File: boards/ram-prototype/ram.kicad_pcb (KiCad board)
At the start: 4 copper layers, 173 x 118 mm, 611 parts, among them J1 PinHeader_1x24_P2.54mm_Vertic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, J2 PinHeader_1x04_P2.54mm_Vertic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, J3 PinHeader_1x14_P2.54mm_Vertic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, J4 PinHeader_2x08_P2.54mm_Vertic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, U1 DSBGA\-5_NumericPads, U10 DSBGA\-5_NumericPads, U100 DSBGA\-5_NumericPads, U101 DSBGA\-5_NumericPads, U102 DSBGA\-5_NumericPads, U103 DSBGA\-5_NumericPads, U104 DSBGA\-5_NumericPads, U105 DSBGA\-5_NumericPads, U106 DSBGA\-5_NumericPads, U107 DSBGA\-5_NumericPads, U108 DSBGA\-5_NumericPads, U109 DSBGA\-5_NumericPads, U11 DSBGA\-5_NumericPads, U110 DSBGA\-5_NumericPads, U111 DSBGA\-5_NumericPads, U112 DSBGA\-5_NumericPads, U113 DSBGA\-5_NumericPads, U114 DSBGA\-5_NumericPads, U115 DSBGA\-5_NumericPads, U116 DSBGA\-5_NumericPads, U117 DSBGA\-5_NumericPads, U118 DSBGA\-5_NumericPads, U119 DSBGA\-5_NumericPads, U12 DSBGA\-5_NumericPads, U120 DSBGA\-5_NumericPads, U121 DSBGA\-5_NumericPads, U122 DSBGA\-5_NumericPads, U123 DSBGA\-5_NumericPads, U124 DSBGA\-5_NumericPads, U125 DSBGA\-5_NumericPads, U126 DSBGA\-5_NumericPads, U127 DSBGA\-5_NumericPads, U128 DSBGA\-5_NumericPads, U129 DSBGA\-5_NumericPads, U13 DSBGA\-5_NumericPads, U130 DSBGA\-5_NumericPads, U131 DSBGA\-5_NumericPads, U132 DSBGA\-5_NumericPads, U133 DSBGA\-5_NumericPads, U134 DSBGA\-5_NumericPads, U135 DSBGA\-5_NumericPads, U136 DSBGA\-5_NumericPads, U137 DSBGA\-5_NumericPads, U138 DSBGA\-5_NumericPads, U139 DSBGA\-5_NumericPads, U14 DSBGA\-5_NumericPads, U140 DSBGA\-5_NumericPads, U141 DSBGA\-5_NumericPads, U142 DSBGA\-5_NumericPads, U143 DSBGA\-5_NumericPads, U144 DSBGA\-5_NumericPads, U145 DSBGA\-5_NumericPads, U146 DSBGA\-5_NumericPads, U147 DSBGA\-5_NumericPads, U148 DSBGA\-5_NumericPads, U149 DSBGA\-5_NumericPads, U15 DSBGA\-5_NumericPads, U150 DSBGA\-5_NumericPads, U151 DSBGA\-5_NumericPads, U152 DSBGA\-5_NumericPads, U153 DSBGA\-5_NumericPads, U154 DSBGA\-5_NumericPads, U155 DSBGA\-5_NumericPads, U156 DSBGA\-5_NumericPads, U157 DSBGA\-5_NumericPads, U158 DSBGA\-5_NumericPads, U159 DSBGA\-5_NumericPads, U16 DSBGA\-5_NumericPads, U160 DSBGA\-5_NumericPads, U161 DSBGA\-5_NumericPads, U162 DSBGA\-5_NumericPads, U163 DSBGA\-5_NumericPads, U164 DSBGA\-5_NumericPads, U165 DSBGA\-5_NumericPads, U166 DSBGA\-5_NumericPads, U167 DSBGA\-5_NumericPads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

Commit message: route D* bus above control logic, restore A7-A10 prerouting
- Move ctrl_logic down 7mm below decoder (CTRL_DBUS_GAP=7.0) to create
  a corridor for the D* bus between decoder bottom and ctrl_logic top
- D* bus corridor at y≈102-106, ctrl_logic at y≈110, A7-A10 below both
- Add obs_y_max filter to preroute_dbus_to_connector so it ignores
  ctrl_logic footprints when computing bus corridor Y
- Restrict obstacle scan to decoder area (x>35) to avoid connector LEDs
- Re-enable A7-A10 prerouting (now clears ctrl_logic)
- Update connector silkscreen labels for swapped pin assignment

Co-Authored-By: Claude Opus 4.6 (1M context) <noreply@anthropic.com>
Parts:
- moved D187 6.90 mm to (47.4, 110.2)
- moved D188 6.90 mm to (52.9, 110.2)
- moved D189 6.90 mm to (58.4, 110.2)
- moved D190 6.90 mm to (52.9, 114.2)
- moved D191 6.90 mm to (47.4, 114.2)
- moved D192 6.90 mm to (58.4, 114.2)
- moved R190 6.90 mm to (48.7, 110.2)
- moved R191 6.90 mm to (54.2, 110.2)
- moved R192 6.90 mm to (59.7, 110.2)
- moved R193 6.90 mm to (54.2, 114.2)
- moved R194 6.90 mm to (48.7, 114.2)
- moved R195 6.90 mm to (59.7, 114.2)
- moved U221 6.90 mm to (45.9, 110.2)
- moved U222 6.90 mm to (51.4, 110.2)
- moved U223 6.90 mm to (56.9, 110.2)
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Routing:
- net /D7: track 100.0 -> 178.4 mm
- net /D6: track 104.5 -> 182.1 mm
- net /D5: track 108.9 -> 185.7 mm
- net /D4: track 113.4 -> 189.4 mm
- net /D3: track 117.9 -> 193.1 mm
- net /D0: track 131.3 -> 206.2 mm
- net /D2: track 122.4 -> 196.8 mm
- net /D1: track 126.8 -> 201.0 mm

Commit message: regenerate all schematics and PCB from scripts
Freshly generated to ensure consistency after rebase.
0 ERC errors/warnings, 0 DRC errors/warnings.

Co-Authored-By: Claude Opus 4.6 (1M context) <noreply@anthropic.com>
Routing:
- net /WRITE_ACTIVE: track 2.67 -> 23.1 mm, vias 0 -> 4
- net /Address Decoder/A0: track 11.6 -> 14.1 mm
- net /Column Select/GA3: track 2.67 -> 4.67 mm
- net /Column Select/GA2: track 2.67 -> 4.67 mm
- net /Column Select/GA1: track 2.67 -> 4.67 mm
- net /Column Select/GA0: track 2.67 -> 4.67 mm
- net /Address Decoder/nA0: track 2.67 -> 4.67 mm
- net /Address Decoder/HA3: track 2.67 -> 4.67 mm
- net /Address Decoder/HA2: track 2.67 -> 4.67 mm
- net /Address Decoder/HA1: track 2.67 -> 4.67 mm
- net /Address Decoder/HA0: track 2.66 -> 4.66 mm
- net /Address Decoder/DEC4_0: track 2.66 -> 4.66 mm
- net /Column Select/A9: track 96.5 -> 98.0 mm
- net /Column Select/A7: track 96.5 -> 98.0 mm
- net /Address Decoder/A5: track 11.6 -> 13.1 mm
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
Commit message: route WRITE_ACTIVE and READ_EN vertical trunks on In1.Cu
Add preroute_ctrl_enable_trunks: routes both control enable signals
from row_ctrl AND gates on In1.Cu vertical trunks.

WRITE_ACTIVE trunk at ic_center_x with gaps where READ_EN horizontal
jogs cross. READ_EN trunk at ic_x+1.24 under the LED+R area. Both
use 0.34mm F.Cu escape stubs from pin 1 to vias with
remove_unused_layers. 8 vias + 25 traces total.

Also adds center escape for DSBGA-5 pin 2 (B1->B2 gap) on AND/INV
ICs (skipping control_logic and row_ctrl groups), and
remove_unused_layers parameter to PCBBuilder.pin_to_via().

0 errors, 0 warnings across Default/PCBWay/Elecrow rulesets.

Co-Authored-By: Claude Opus 4.6 (1M context) <noreply@anthropic.com>
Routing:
- net /READ_EN: track 2.67 -> 24.6 mm, vias 0 -> 4
- net /WRITE_ACTIVE: track 23.1 -> 18.7 mm
- net /nWE: track 12.6 -> 11.6 mm
- net /Address Decoder/ROW_SEL_3: track 3.67 -> 2.67 mm
- net /Address Decoder/ROW_SEL_2: track 3.67 -> 2.67 mm
- net /Address Decoder/ROW_SEL_1: track 3.66 -> 2.66 mm
- net /Address Decoder/ROW_SEL_0: track 3.66 -> 2.66 mm
- net Net-(D189-A): track 3.17 -> 2.67 mm
- net Net-(D188-A): track 3.17 -> 2.67 mm
- net /nOE: track 12.1 -> 11.6 mm
- net /nCE: track 12.1 -> 11.6 mm

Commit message: add pin 2 escape stubs for row_ctrl/control_logic, fix WRITE_ACTIVE trunk, improve FreeRouting clearances
- Remove skip of control_logic and row_ctrl ICs from preroute_center_escape
  so pin 2 (middle ball) gets escape stubs — reduces unconnected items from
  176 to 15
- Move READ_EN vias right of WRITE_ACTIVE trunk so horizontal jogs don't
  cross it, making WRITE_ACTIVE one uninterrupted vertical line
- Add Connectors net class for J2/J3/J4 secondary headers in .kicad_pro
- Fix DSN clearances: smd_smd 37.5µm→150µm, add via_via/via_smd/via_pin
  250µm to match KiCad DRC settings
- Increase verify timeout from 120s to 600s

Co-Authored-By: Claude Opus 4.6 (1M context) <noreply@anthropic.com>
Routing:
- net /WRITE_ACTIVE: track 18.7 -> 21.7 mm
- net /nWE: track 11.6 -> 12.6 mm
- net /Address Decoder/ROW_SEL_3: track 2.67 -> 3.67 mm
- net /Address Decoder/ROW_SEL_2: track 2.67 -> 3.67 mm
- net /Address Decoder/ROW_SEL_1: track 2.66 -> 3.66 mm
- net /Address Decoder/ROW_SEL_0: track 2.66 -> 3.66 mm
- net /READ_EN: track 24.6 -> 24.0 mm
- net Net-(D189-A): track 2.67 -> 3.17 mm
- net Net-(D188-A): track 2.67 -> 3.17 mm
- net /nOE: track 11.6 -> 12.1 mm
- net /nCE: track 11.6 -> 12.1 mm
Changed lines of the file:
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@@
   (segment (start 73.11 72.01) (end 72.61 72.01) (width 0.2) (layer "F.Cu") (net 12))
   (segment (start 73.11 77.56) (end 72.61 77.56) (width 0.2) (layer "F.Cu") (net 12))
+  (segment (start 86.41 60.91) (end 85.91 60.91) (width 0.2) (layer "F.Cu") (net 25))
+  (segment (start 86.41 63.21) (end 85.91 63.21) (width 0.2) (layer "F.Cu") (net 25))
+  (segment (start 86.41 66.46) (end 85.91 66.46) (width 0.2) (layer "F.Cu") (net 26))
+  (segment (start 86.41 68.76) (end 85.91 68.76) (width 0.2) (layer "F.Cu") (net 26))
+  (segment (start 86.41 72.01) (end 85.91 72.01) (width 0.2) (layer "F.Cu") (net 27))
+  (segment (start 86.41 74.31) (end 85.91 74.31) (width 0.2) (layer "F.Cu") (net 27))
+  (segment (start 86.41 77.56) (end 85.91 77.56) (width 0.2) (layer "F.Cu") (net 28))
+  (segment (start 86.41 79.86) (end 85.91 79.86) (width 0.2) (layer "F.Cu") (net 28))
+  (segment (start 46.11 110.23) (end 45.61 110.23) (width 0.2) (layer "F.Cu") (net 102))
+  (segment (start 51.61 110.23) (end 51.11 110.23) (width 0.2) (layer "F.Cu") (net 103))
+  (segment (start 57.11 110.23) (end 56.61 110.23) (width 0.2) (layer "F.Cu") (net 104))
+  (segment (start 46.11 114.23) (end 45.61 114.23) (width 0.2) (layer "F.Cu") (net 382))
+  (segment (start 51.61 114.23) (end 51.11 114.23) (width 0.2) (layer "F.Cu") (net 380))
+  (segment (start 57.11 114.23) (end 56.61 114.23) (width 0.2) (layer "F.Cu") (net 104))
   (segment (start 127.86 113.75) (end 127.86 114.25) (width 0.2) (layer "F.Cu") (net 52))
   (segment (start 131.86 113.75) (end 131.86 114.25) (width 0.2) (layer "F.Cu") (net 53))
@@
   (via (at 86.41 80.7) (size 0.5) (drill 0.3) (layers "F.Cu" "In1.Cu") (remove_unused_layers yes) (net 97))
   (segment (start 86.41 80.7) (end 86.16 80.7) (width 0.16) (layer "In1.Cu") (net 97))
-  (segment (start 86.41 61.41) (end 86.41 61.75) (width 0.2) (layer "F.Cu") (net 92))
-  (via (at 86.41 61.75) (size 0.5) (drill 0.3) (layers "F.Cu" "In1.Cu") (remove_unused_layers yes) (net 92))
-  (segment (start 86.41 61.75) (end 87.4 61.75) (width 0.16) (layer "In1.Cu") (net 92))
-  (segment (start 86.41 66.96) (end 86.41 67.3) (width 0.2) (layer "F.Cu") (net 92))
-  (via (at 86.41 67.3) (size 0.5) (drill 0.3) (layers "F.Cu" "In1.Cu") (remove_unused_layers yes) (net 92))
-  (segment (start 86.41 67.3) (end 87.4 67.3) (width 0.16) (layer "In1.Cu") (net 92))
-  (segment (start 86.41 72.51) (end 86.41 72.85) (width 0.2) (layer "F.Cu") (net 92))
-  (via (at 86.41 72.85) (size 0.5) (drill 0.3) (layers "F.Cu" "In1.Cu") (remove_unused_layers yes) (net 92))
-  (segment (start 86.41 72.85) (end 87.4 72.85) (width 0.16) (layer "In1.Cu") (net 92))
-  (segment (start 86.41 78.06) (end 86.41 78.4) (width 0.2) (layer "F.Cu") (net 92))
-  (via (at 86.41 78.4) (size 0.5) (drill 0.3) (layers "F.Cu" "In1.Cu") (remove_unused_layers yes) (net 92))
-  (segment (start 86.41 78.4) (end 87.4 78.4) (width 0.16) (layer "In1.Cu") (net 92))
-  (segment (start 86.16 64.05) (end 86.16 66.81) (width 0.16) (layer "In1.Cu") (net 97))
-  (segment (start 86.16 67.79) (end 86.16 69.6) (width 0.16) (layer "In1.Cu") (net 97))
-  (segment (start 86.16 69.6) (end 86.16 72.36) (width 0.16) (layer "In1.Cu") (net 97))
-  (segment (start 86.16 73.34) (end 86.16 75.15) (width 0.16) (layer "In1.Cu") (net 97))
-  (segment (start 86.16 75.15) (end 86.16 77.91) (width 0.16) (layer "In1.Cu") (net 97))
-  (segment (start 86.16 78.89) (end 86.16 80.7) (width 0.16) (layer "In1.Cu") (net 97))
+  (segment (start 86.41 61.41) (end 86.66 61.75) (width 0.2) (layer "F.Cu") (net 92))
+  (via (at 86.66 61.75) (size 0.5) (drill 0.3) (layers "F.Cu" "In1.Cu") (remove_unused_layers yes) (net 92))
+  (segment (start 86.66 61.75) (end 87.4 61.75) (width 0.16) (layer "In1.Cu") (net 92))
+  (segment (start 86.41 66.96) (end 86.66 67.3) (width 0.2) (layer "F.Cu") (net 92))
+  (via (at 86.66 67.3) (size 0.5) (drill 0.3) (layers "F.Cu" "In1.Cu") (remove_unused_layers yes) (net 92))
+  (segment (start 86.66 67.3) (end 87.4 67.3) (width 0.16) (layer "In1.Cu") (net 92))
+  (segment (start 86.41 72.51) (end 86.66 72.85) (width 0.2) (layer "F.Cu") (net 92))
+  (via (at 86.66 72.85) (size 0.5) (drill 0.3) (layers "F.Cu" "In1.Cu") (remove_unused_layers yes) (net 92))
+  (segment (start 86.66 72.85) (end 87.4 72.85) (width 0.16) (layer "In1.Cu") (net 92))
+  (segment (start 86.41 78.06) (end 86.66 78.4) (width 0.2) (layer "F.Cu") (net 92))
+  (via (at 86.66 78.4) (size 0.5) (drill 0.3) (layers "F.Cu" "In1.Cu") (remove_unused_layers yes) (net 92))
+  (segment (start 86.66 78.4) (end 87.4 78.4) (width 0.16) (layer "In1.Cu") (net 92))
+  (segment (start 86.16 64.05) (end 86.16 69.6) (width 0.16) (layer "In1.Cu") (net 97))
+  (segment (start 86.16 69.6) (end 86.16 75.15) (width 0.16) (layer "In1.Cu") (net 97))
+  (segment (start 86.16 75.15) (end 86.16 80.7) (width 0.16) (layer "In1.Cu") (net 97))
   (segment (start 87.4 61.75) (end 87.4 67.3) (width 0.16) (layer "In1.Cu") (net 92))
   (segment (start 87.4 67.3) (end 87.4 72.85) (width 0.16) (layer "In1.Cu") (net 92))

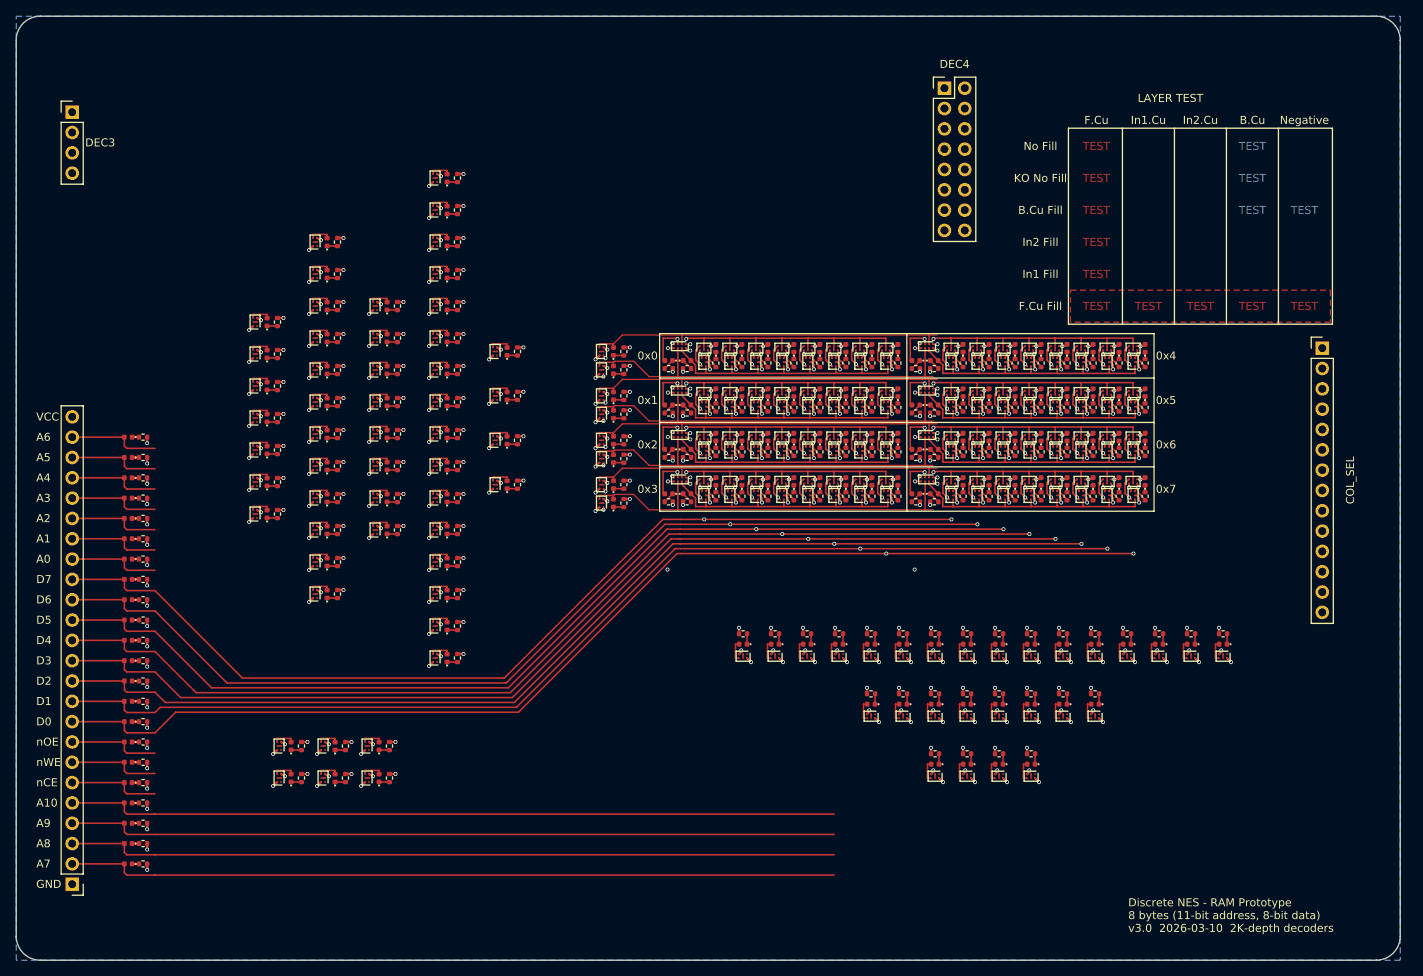
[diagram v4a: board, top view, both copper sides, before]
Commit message: fix pad coordinate precision, extend ram keepout, match fab clearance rules
- Increase get_pad_position() and add_trace() precision from 2 to 3 decimals
  (0.01mm -> 0.001mm). Fixes 5µm mismatch between trace endpoints and DSBGA
  pad positions that caused dangling track cleanup to delete NAND LED traces
- Extend ram_grid routing keepout to cover D* bus horizontal traces below
  byte grid (y2: 81.38 -> 86.67), stops before COL_SEL vias
- Match DSN clearances to actual PCBWay/Elecrow fab rules: via-to-track and
  via-to-via use 10mil (0.254mm) not 0.25mm. Eliminates all hole_clearance
  DRC violations. Post-routing errors: 271 -> 36

Co-Authored-By: Claude Opus 4.6 (1M context) <noreply@anthropic.com>
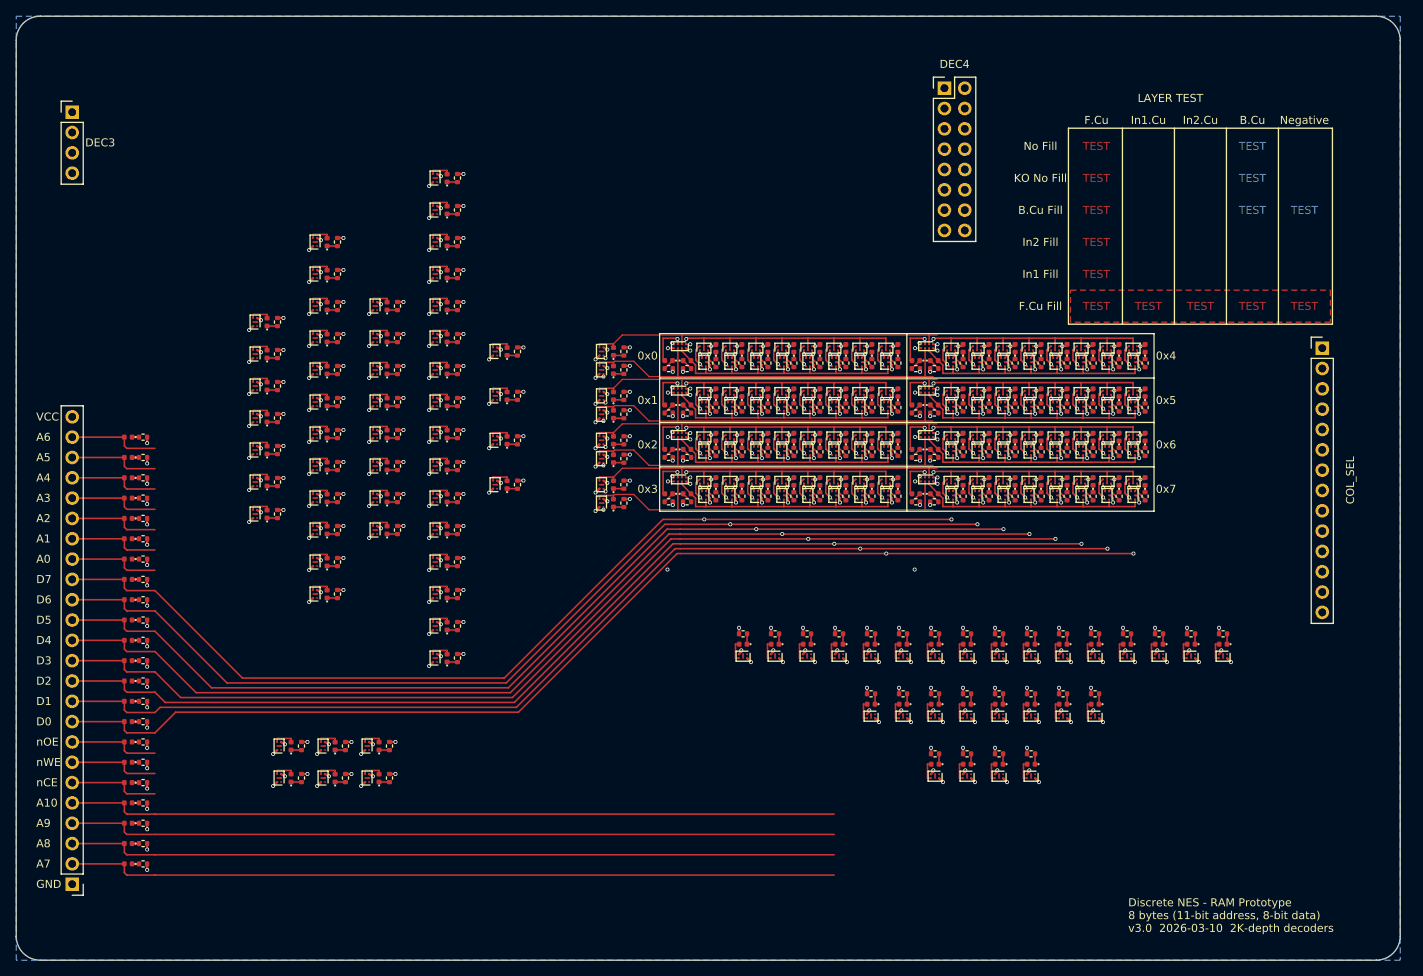
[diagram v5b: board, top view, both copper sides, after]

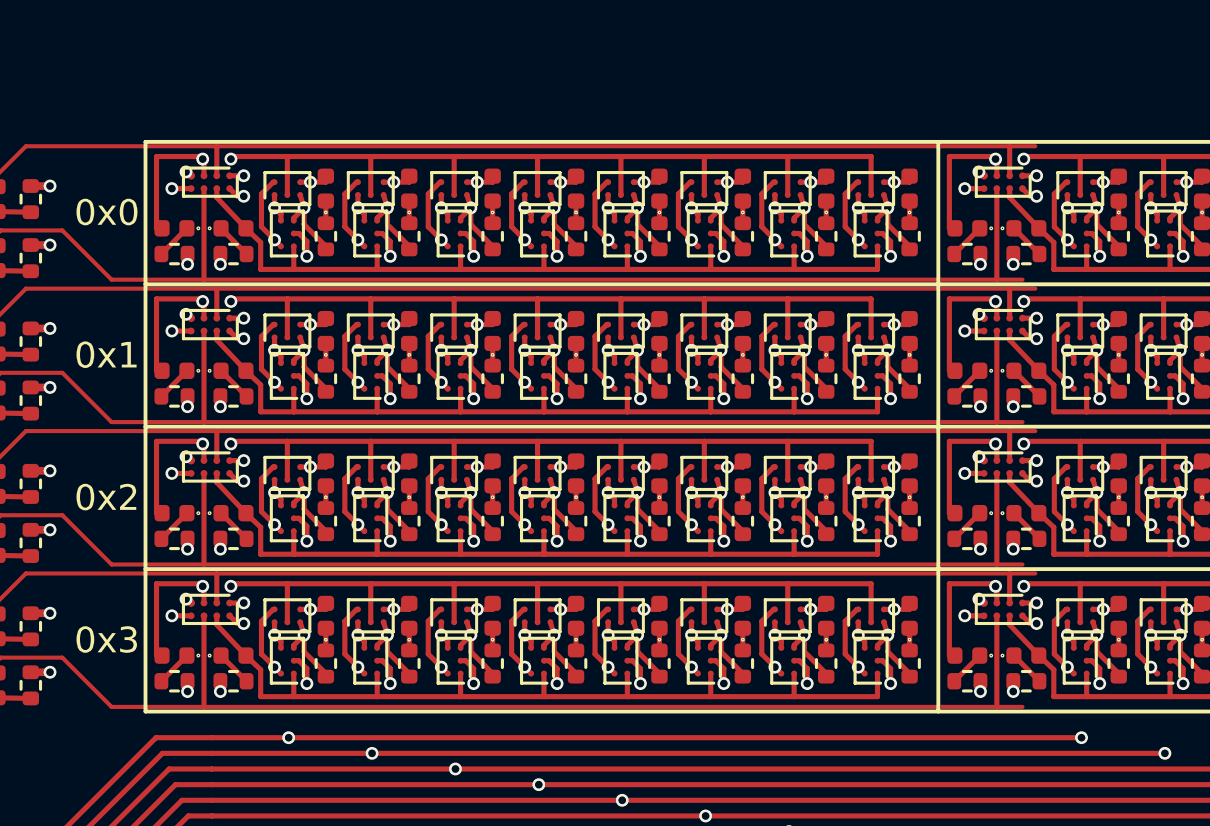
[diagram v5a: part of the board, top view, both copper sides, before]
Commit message: fix NAND LED anode route, COL_SEL trunk gap, and pad index precision
- Fix CLK LED approach route: T-branch from clk_pos[0] instead of
  clk_via_x (0.05mm gap caused dangling cleanup to delete LED route)
- Fix COL_SEL trunk extension: use actual bottom pin Y from
  get_pad_position() instead of hardcoded crtyd_bot_y (0.55mm gap)
- Increase _build_net_pad_index precision to 3 decimals to match
  get_pad_position/add_trace precision
- Save raw post-SES-import PCB to verify_output/ for inspection
- Post-routing: 36 errors -> 3 (1 nCE unconnected + 2 solder mask)

Co-Authored-By: Claude Opus 4.6 (1M context) <noreply@anthropic.com>
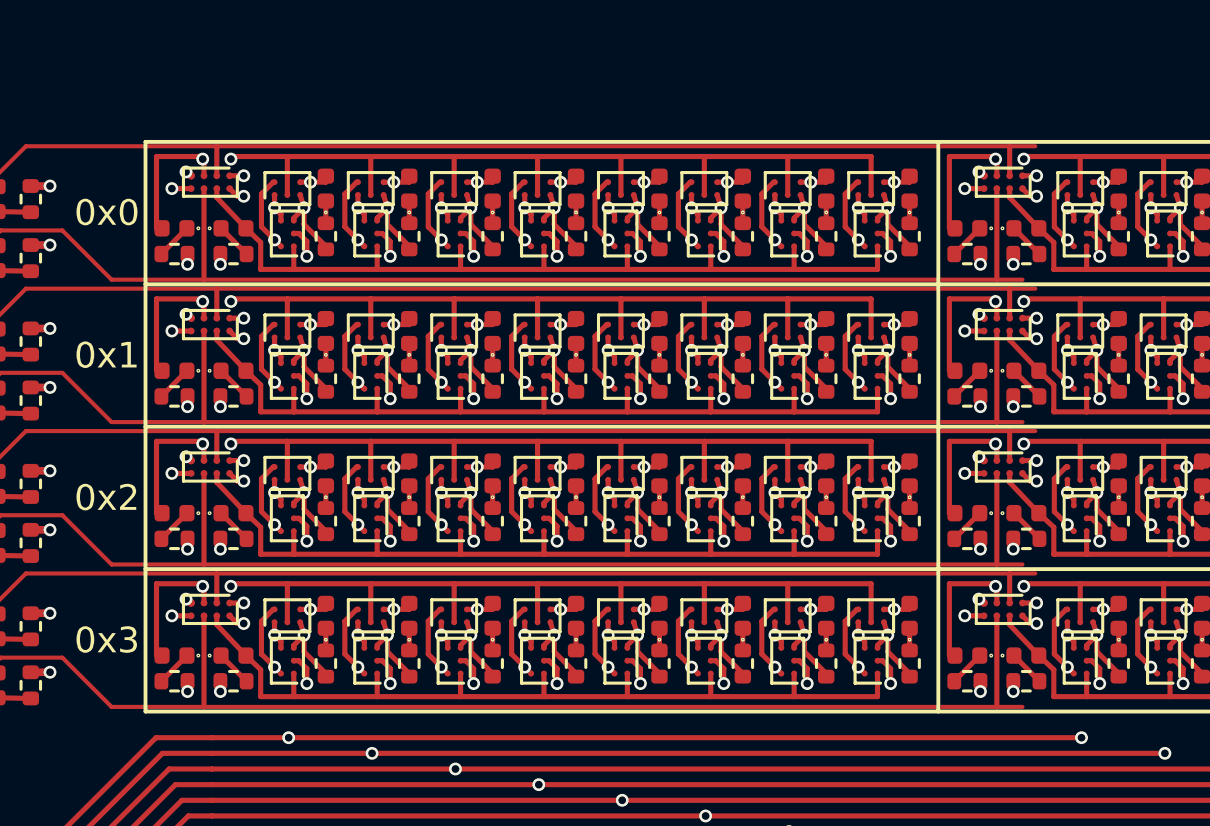
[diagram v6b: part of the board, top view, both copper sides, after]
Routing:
- net /COL_SEL_1: track 47.2 -> 47.8 mm
- net /COL_SEL_0: track 47.2 -> 47.8 mm
